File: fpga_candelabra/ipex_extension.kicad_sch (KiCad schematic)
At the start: 5 parts

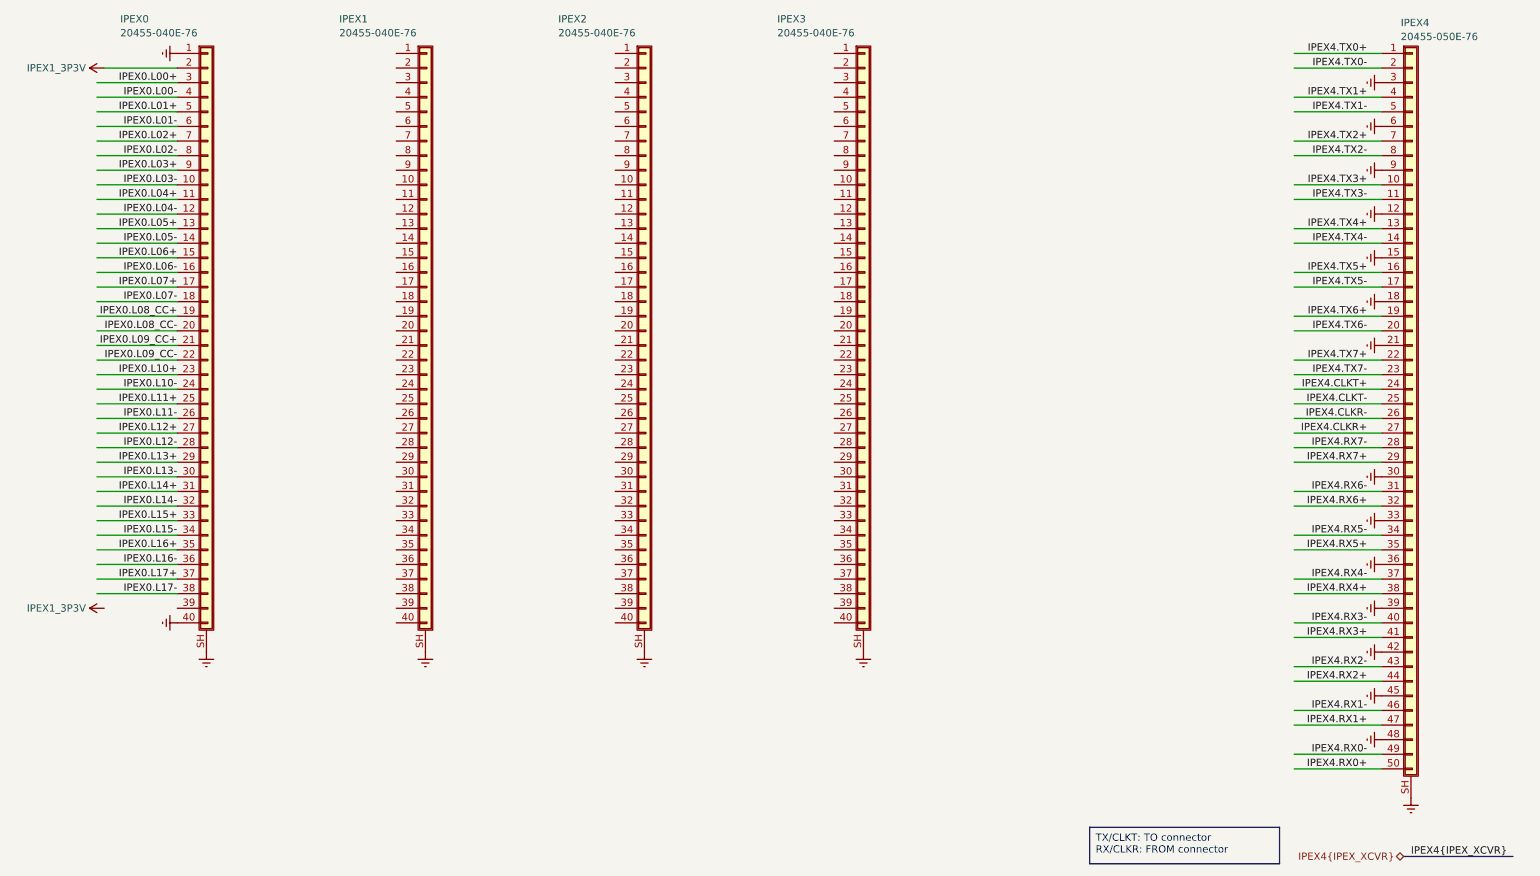
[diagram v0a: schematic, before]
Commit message: fpga_candelabra: major revision
* Finish DDR4 & QSFP+ & PCIe layout
* Change FMC to LPC
* Add mikroBUS extension
* 12V input & PDN updates
* FPGA config updates

Signed-off-by: Yichuan Gao <gaoyichuan000@gmail.com>
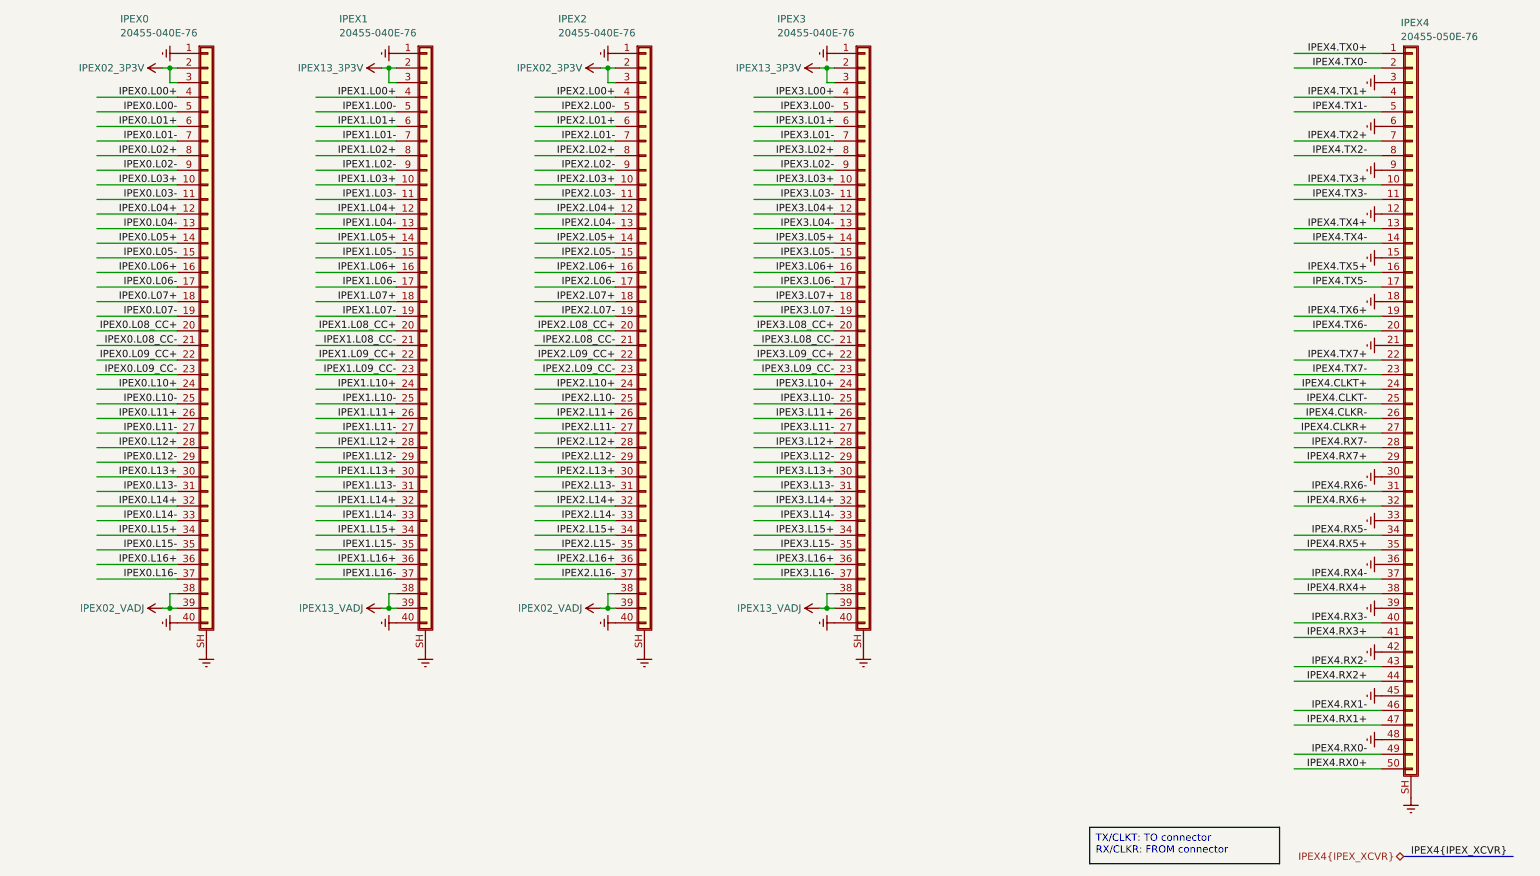
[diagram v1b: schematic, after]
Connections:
- net IPEX0.L17+ is gone; now on net IPEX0.L16-: IPEX0.37 (Pin_37)
- net IPEX0.L17- is gone; now on net IPEX02_VADJ: IPEX0.38 (Pin_38)
- net IPEX1_3P3V is gone; now on net IPEX02_3P3V: IPEX0.2 (Pin_2)
- net Earth: now also IPEX1.1 (Pin_1), IPEX1.40 (Pin_40), IPEX2.1 (Pin_1), IPEX2.40 (Pin_40), IPEX3.1 (Pin_1), IPEX3.40 (Pin_40)
- net IPEX0.L00+: now also IPEX0.4 (Pin_4); no longer IPEX0.3 (Pin_3)
- net IPEX0.L00-: now also IPEX0.5 (Pin_5); no longer IPEX0.4 (Pin_4)
- net IPEX0.L01+: now also IPEX0.6 (Pin_6); no longer IPEX0.5 (Pin_5)
- net IPEX0.L01-: now also IPEX0.7 (Pin_7); no longer IPEX0.6 (Pin_6)
- net IPEX0.L02+: now also IPEX0.8 (Pin_8); no longer IPEX0.7 (Pin_7)
- net IPEX0.L02-: now also IPEX0.9 (Pin_9); no longer IPEX0.8 (Pin_8)
- net IPEX0.L03+: now also IPEX0.10 (Pin_10); no longer IPEX0.9 (Pin_9)
- net IPEX0.L03-: now also IPEX0.11 (Pin_11); no longer IPEX0.10 (Pin_10)
- net IPEX0.L04+: now also IPEX0.12 (Pin_12); no longer IPEX0.11 (Pin_11)
- net IPEX0.L04-: now also IPEX0.13 (Pin_13); no longer IPEX0.12 (Pin_12)
- net IPEX0.L05+: now also IPEX0.14 (Pin_14); no longer IPEX0.13 (Pin_13)
- net IPEX0.L05-: now also IPEX0.15 (Pin_15); no longer IPEX0.14 (Pin_14)
- net IPEX0.L06+: now also IPEX0.16 (Pin_16); no longer IPEX0.15 (Pin_15)
- net IPEX0.L06-: now also IPEX0.17 (Pin_17); no longer IPEX0.16 (Pin_16)
- net IPEX0.L07+: now also IPEX0.18 (Pin_18); no longer IPEX0.17 (Pin_17)
- net IPEX0.L07-: now also IPEX0.19 (Pin_19); no longer IPEX0.18 (Pin_18)
- net IPEX0.L08_CC+: now also IPEX0.20 (Pin_20); no longer IPEX0.19 (Pin_19)
- net IPEX0.L08_CC-: now also IPEX0.21 (Pin_21); no longer IPEX0.20 (Pin_20)
- net IPEX0.L09_CC+: now also IPEX0.22 (Pin_22); no longer IPEX0.21 (Pin_21)
- net IPEX0.L09_CC-: now also IPEX0.23 (Pin_23); no longer IPEX0.22 (Pin_22)
- net IPEX0.L10+: now also IPEX0.24 (Pin_24); no longer IPEX0.23 (Pin_23)
- net IPEX0.L10-: now also IPEX0.25 (Pin_25); no longer IPEX0.24 (Pin_24)
- net IPEX0.L11+: now also IPEX0.26 (Pin_26); no longer IPEX0.25 (Pin_25)
- net IPEX0.L11-: now also IPEX0.27 (Pin_27); no longer IPEX0.26 (Pin_26)
- net IPEX0.L12+: now also IPEX0.28 (Pin_28); no longer IPEX0.27 (Pin_27)
- net IPEX0.L12-: now also IPEX0.29 (Pin_29); no longer IPEX0.28 (Pin_28)
- net IPEX0.L13+: now also IPEX0.30 (Pin_30); no longer IPEX0.29 (Pin_29)
- net IPEX0.L13-: now also IPEX0.31 (Pin_31); no longer IPEX0.30 (Pin_30)
- net IPEX0.L14+: now also IPEX0.32 (Pin_32); no longer IPEX0.31 (Pin_31)
- net IPEX0.L14-: now also IPEX0.33 (Pin_33); no longer IPEX0.32 (Pin_32)
- net IPEX0.L15+: now also IPEX0.34 (Pin_34); no longer IPEX0.33 (Pin_33)
- net IPEX0.L15-: now also IPEX0.35 (Pin_35); no longer IPEX0.34 (Pin_34)
- net IPEX0.L16+: now also IPEX0.36 (Pin_36); no longer IPEX0.35 (Pin_35)
- net IPEX0.L16-: no longer IPEX0.36 (Pin_36)
- net IPEX1.L03+: now reaches IPEX1.10 (Pin_10)
- net IPEX1.L03-: now reaches IPEX1.11 (Pin_11)
- net IPEX1.L04+: now reaches IPEX1.12 (Pin_12)
- net IPEX1.L04-: now reaches IPEX1.13 (Pin_13)
- net IPEX1.L05+: now reaches IPEX1.14 (Pin_14)
- net IPEX1.L05-: now reaches IPEX1.15 (Pin_15)
- net IPEX1.L06+: now reaches IPEX1.16 (Pin_16)
- net IPEX1.L06-: now reaches IPEX1.17 (Pin_17)
- net IPEX1.L07+: now reaches IPEX1.18 (Pin_18)
- net IPEX1.L07-: now reaches IPEX1.19 (Pin_19)
- net IPEX13_3P3V: now reaches IPEX1.2 (Pin_2)
- net IPEX13_3P3V: now also IPEX1.3 (Pin_3), IPEX3.2 (Pin_2), IPEX3.3 (Pin_3)
- net IPEX1.L08_CC+: now reaches IPEX1.20 (Pin_20)
- net IPEX1.L08_CC-: now reaches IPEX1.21 (Pin_21)
- net IPEX1.L09_CC+: now reaches IPEX1.22 (Pin_22)
- net IPEX1.L09_CC-: now reaches IPEX1.23 (Pin_23)
- net IPEX1.L10+: now reaches IPEX1.24 (Pin_24)
- net IPEX1.L10-: now reaches IPEX1.25 (Pin_25)
- net IPEX1.L11+: now reaches IPEX1.26 (Pin_26)
- net IPEX1.L11-: now reaches IPEX1.27 (Pin_27)
- net IPEX1.L12+: now reaches IPEX1.28 (Pin_28)
- net IPEX1.L12-: now reaches IPEX1.29 (Pin_29)
- net IPEX1.L13+: now reaches IPEX1.30 (Pin_30)
- net IPEX1.L13-: now reaches IPEX1.31 (Pin_31)
- net IPEX1.L14+: now reaches IPEX1.32 (Pin_32)
- net IPEX1.L14-: now reaches IPEX1.33 (Pin_33)
- net IPEX1.L15+: now reaches IPEX1.34 (Pin_34)
- net IPEX1.L15-: now reaches IPEX1.35 (Pin_35)
- net IPEX1.L16+: now reaches IPEX1.36 (Pin_36)
- net IPEX1.L16-: now reaches IPEX1.37 (Pin_37)
- net IPEX13_VADJ: now reaches IPEX1.38 (Pin_38)
- net IPEX13_VADJ: now also IPEX1.39 (Pin_39), IPEX3.38 (Pin_38), IPEX3.39 (Pin_39)
- net IPEX1.L00+: now reaches IPEX1.4 (Pin_4)
- net IPEX1.L00-: now reaches IPEX1.5 (Pin_5)
- net IPEX1.L01+: now reaches IPEX1.6 (Pin_6)
- net IPEX1.L01-: now reaches IPEX1.7 (Pin_7)
- net IPEX1.L02+: now reaches IPEX1.8 (Pin_8)
- net IPEX1.L02-: now reaches IPEX1.9 (Pin_9)
- net IPEX3.L03+: now reaches IPEX3.10 (Pin_10)
- net IPEX3.L03-: now reaches IPEX3.11 (Pin_11)
- net IPEX3.L04+: now reaches IPEX3.12 (Pin_12)
- net IPEX3.L04-: now reaches IPEX3.13 (Pin_13)
- net IPEX3.L05+: now reaches IPEX3.14 (Pin_14)
- net IPEX3.L05-: now reaches IPEX3.15 (Pin_15)
- net IPEX3.L06+: now reaches IPEX3.16 (Pin_16)
- net IPEX3.L06-: now reaches IPEX3.17 (Pin_17)
- net IPEX3.L07+: now reaches IPEX3.18 (Pin_18)
- net IPEX3.L07-: now reaches IPEX3.19 (Pin_19)
- net IPEX3.L08_CC+: now reaches IPEX3.20 (Pin_20)
- net IPEX3.L08_CC-: now reaches IPEX3.21 (Pin_21)
- net IPEX3.L09_CC+: now reaches IPEX3.22 (Pin_22)
- net IPEX3.L09_CC-: now reaches IPEX3.23 (Pin_23)
- net IPEX3.L10+: now reaches IPEX3.24 (Pin_24)
- net IPEX3.L10-: now reaches IPEX3.25 (Pin_25)
- net IPEX3.L11+: now reaches IPEX3.26 (Pin_26)
- net IPEX3.L11-: now reaches IPEX3.27 (Pin_27)
- net IPEX3.L12+: now reaches IPEX3.28 (Pin_28)
- net IPEX3.L12-: now reaches IPEX3.29 (Pin_29)
- net IPEX3.L13+: now reaches IPEX3.30 (Pin_30)
- net IPEX3.L13-: now reaches IPEX3.31 (Pin_31)
- net IPEX3.L14+: now reaches IPEX3.32 (Pin_32)
- net IPEX3.L14-: now reaches IPEX3.33 (Pin_33)
- net IPEX3.L15+: now reaches IPEX3.34 (Pin_34)
- net IPEX3.L15-: now reaches IPEX3.35 (Pin_35)
- net IPEX3.L16+: now reaches IPEX3.36 (Pin_36)
- net IPEX3.L16-: now reaches IPEX3.37 (Pin_37)
- net IPEX3.L00+: now reaches IPEX3.4 (Pin_4)
- net IPEX3.L00-: now reaches IPEX3.5 (Pin_5)
- net IPEX3.L01+: now reaches IPEX3.6 (Pin_6)
- net IPEX3.L01-: now reaches IPEX3.7 (Pin_7)
- net IPEX3.L02+: now reaches IPEX3.8 (Pin_8)
- net IPEX3.L02-: now reaches IPEX3.9 (Pin_9)
- net IPEX2.L03+: now reaches IPEX2.10 (Pin_10)
- net IPEX2.L03-: now reaches IPEX2.11 (Pin_11)
- net IPEX2.L04+: now reaches IPEX2.12 (Pin_12)
- net IPEX2.L04-: now reaches IPEX2.13 (Pin_13)
- net IPEX2.L05+: now reaches IPEX2.14 (Pin_14)
- net IPEX2.L05-: now reaches IPEX2.15 (Pin_15)
- net IPEX2.L06+: now reaches IPEX2.16 (Pin_16)
- net IPEX2.L06-: now reaches IPEX2.17 (Pin_17)
- net IPEX2.L07+: now reaches IPEX2.18 (Pin_18)
- net IPEX2.L07-: now reaches IPEX2.19 (Pin_19)
- net IPEX02_3P3V: now reaches IPEX2.2 (Pin_2)
- net IPEX02_3P3V: now also IPEX0.3 (Pin_3), IPEX2.3 (Pin_3)
- net IPEX2.L08_CC+: now reaches IPEX2.20 (Pin_20)
- net IPEX2.L08_CC-: now reaches IPEX2.21 (Pin_21)
- net IPEX2.L09_CC+: now reaches IPEX2.22 (Pin_22)
- net IPEX2.L09_CC-: now reaches IPEX2.23 (Pin_23)
- net IPEX2.L10+: now reaches IPEX2.24 (Pin_24)
- net IPEX2.L10-: now reaches IPEX2.25 (Pin_25)
- net IPEX2.L11+: now reaches IPEX2.26 (Pin_26)
- net IPEX2.L11-: now reaches IPEX2.27 (Pin_27)
- net IPEX2.L12+: now reaches IPEX2.28 (Pin_28)
- net IPEX2.L12-: now reaches IPEX2.29 (Pin_29)
- net IPEX2.L13+: now reaches IPEX2.30 (Pin_30)
- net IPEX2.L13-: now reaches IPEX2.31 (Pin_31)
- net IPEX2.L14+: now reaches IPEX2.32 (Pin_32)
- net IPEX2.L14-: now reaches IPEX2.33 (Pin_33)
- net IPEX2.L15+: now reaches IPEX2.34 (Pin_34)
- net IPEX2.L15-: now reaches IPEX2.35 (Pin_35)
- net IPEX2.L16+: now reaches IPEX2.36 (Pin_36)
- net IPEX2.L16-: now reaches IPEX2.37 (Pin_37)
- net IPEX02_VADJ: now reaches IPEX2.38 (Pin_38)
- net IPEX02_VADJ: now also IPEX0.39 (Pin_39), IPEX2.39 (Pin_39)
- net IPEX2.L00+: now reaches IPEX2.4 (Pin_4)
- net IPEX2.L00-: now reaches IPEX2.5 (Pin_5)
- net IPEX2.L01+: now reaches IPEX2.6 (Pin_6)
- net IPEX2.L01-: now reaches IPEX2.7 (Pin_7)
- net IPEX2.L02+: now reaches IPEX2.8 (Pin_8)
- net IPEX2.L02-: now reaches IPEX2.9 (Pin_9)
